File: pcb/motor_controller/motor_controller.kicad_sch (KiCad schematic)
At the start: 0 parts

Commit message: Started making symbols for motor driver.
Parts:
- added U1: STM32F446RETx, Package_QFP:LQFP-64_10x10mm_P0.5mm, symbol MCU_ST_STM32F4:STM32F446RETx
- added U2: MCP2542FDxMF, Package_DFN_QFN:DFN-8-1EP_3x3mm_P0.65mm_EP1.55x2.4mm, symbol Interface_CAN_LIN:MCP2542FDxMF
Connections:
- new net: U2.2 (VSS), U2.9 (VSS)
- new net: U1.18 (VSS), U1.31 (VSS), U1.47 (VSS), U1.63 (VSS)

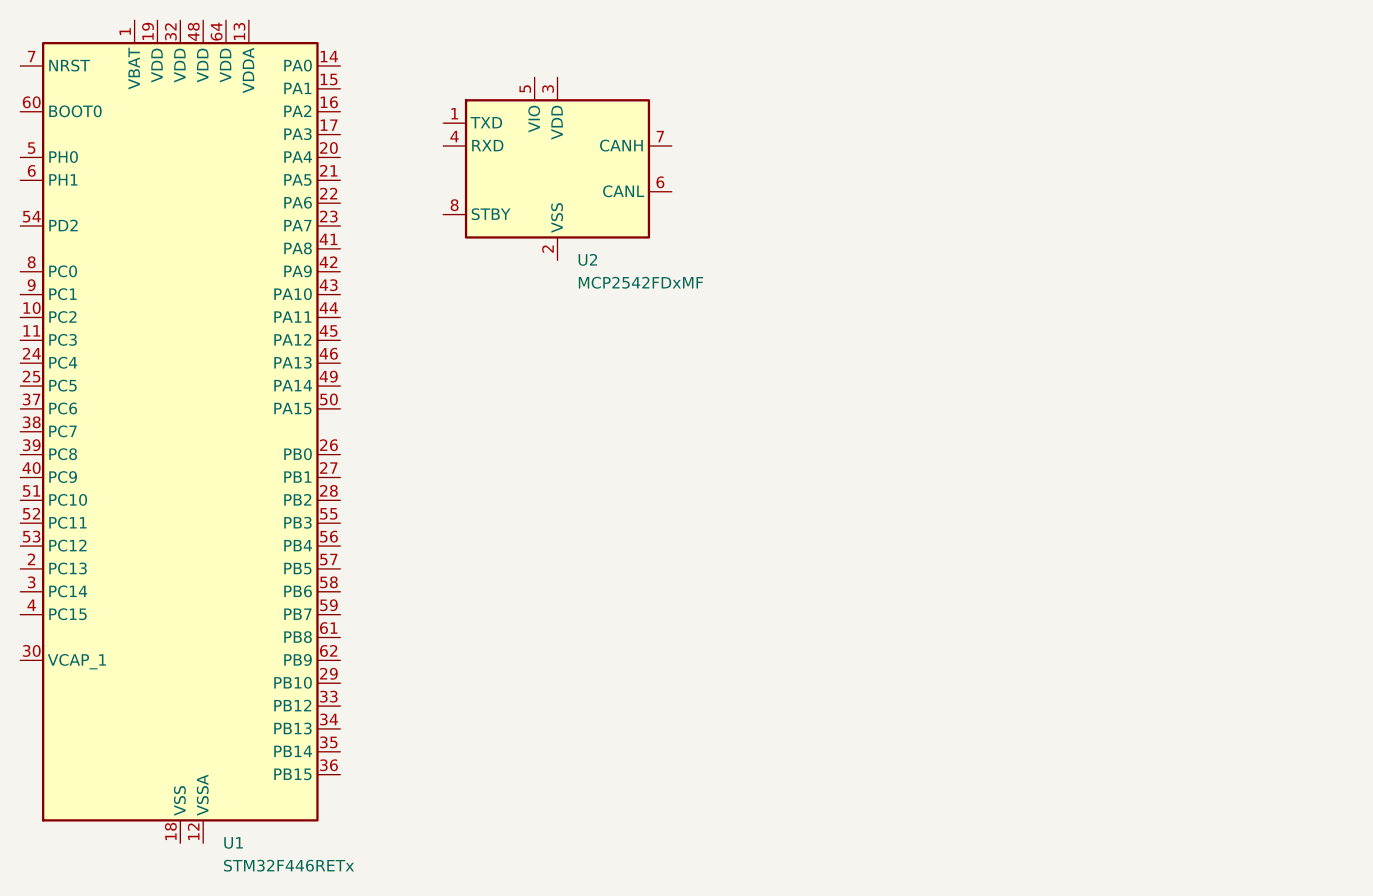
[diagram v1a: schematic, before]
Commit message: Finished all integrated circuit symbols.
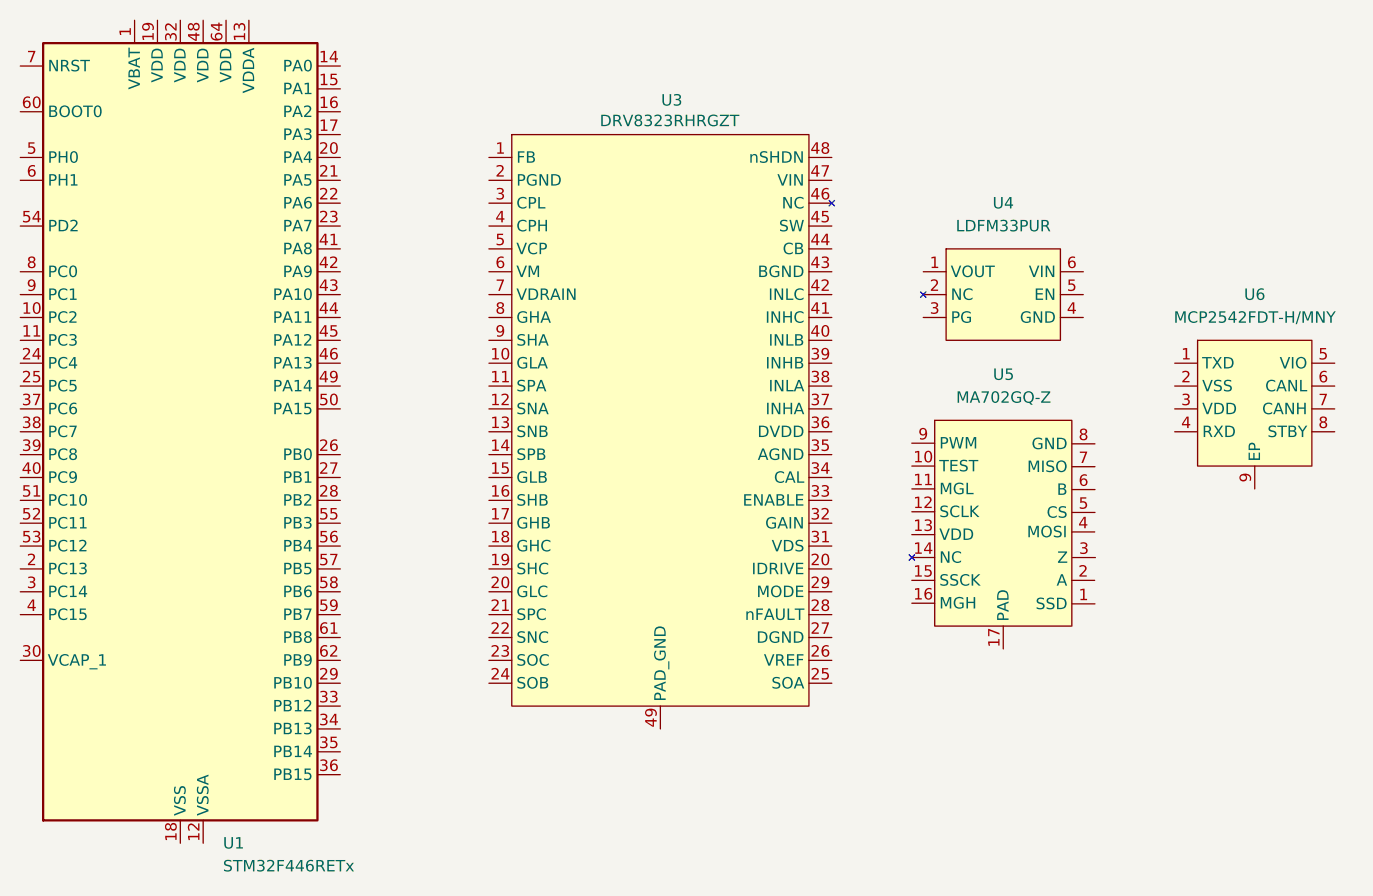
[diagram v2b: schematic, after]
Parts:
- removed U2: MCP2542FDxMF, Package_DFN_QFN:DFN-8-1EP_3x3mm_P0.65mm_EP1.55x2.4mm, symbol Interface_CAN_LIN:MCP2542FDxMF
- added U3: DRV8323RHRGZT, symbol motor_controller_symbols:DRV8323RHRGZT
- added U4: LDFM33PUR, symbol motor_controller_symbols:LDFM33PUR
- added U5: MA702GQ-Z, symbol motor_controller_symbols:MA702GQ-Z
- added U6: MCP2542FDT-H/MNY, symbol motor_controller_symbols:MCP2542FDT-H/MNY
